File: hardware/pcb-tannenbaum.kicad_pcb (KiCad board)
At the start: 2 copper layers, 70 x 89 mm, 30 parts, among them J1 Conn_02x03_Counter_Clockwise, SW1 SW_Push, SW2 SW_Push, U1 TMP101, U2 ATtiny85V-10SU, U3 TPS27081A_ForReversePolarityP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

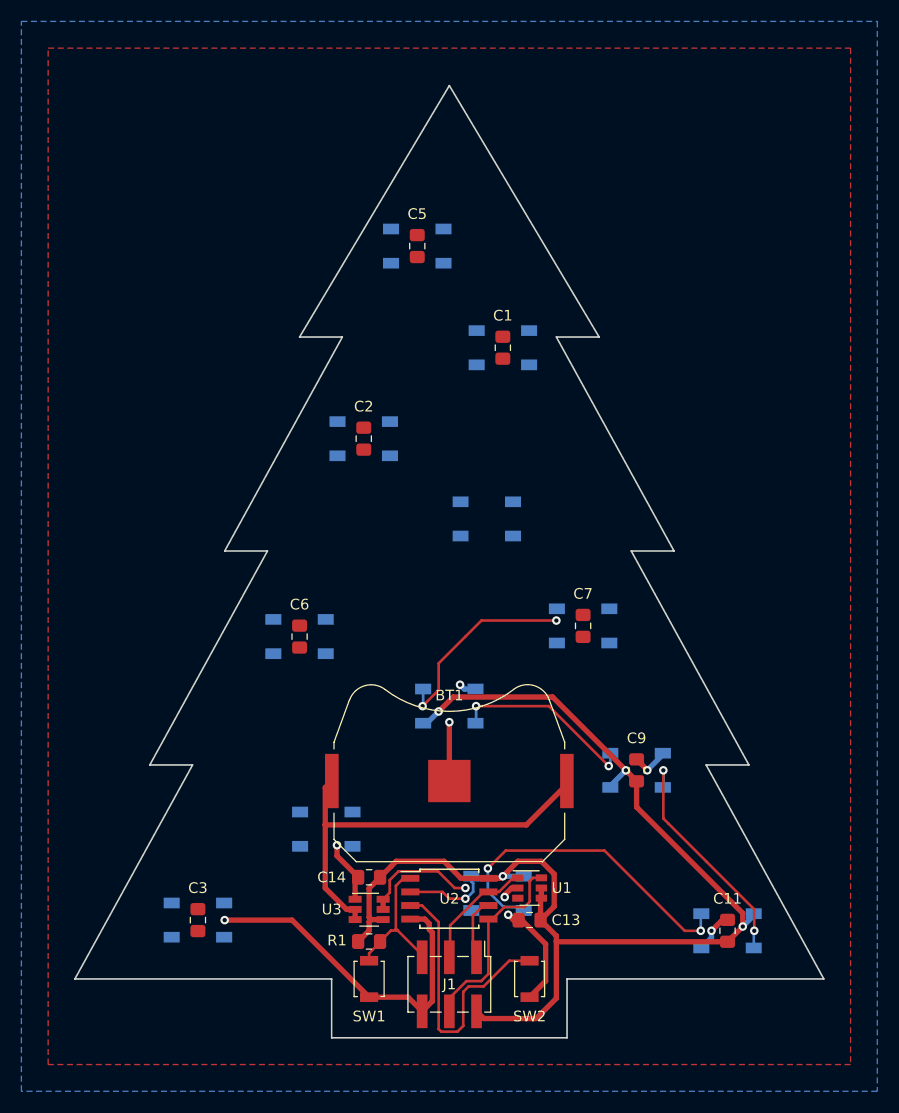
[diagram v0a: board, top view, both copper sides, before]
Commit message: Finish first iteration of PCB layout
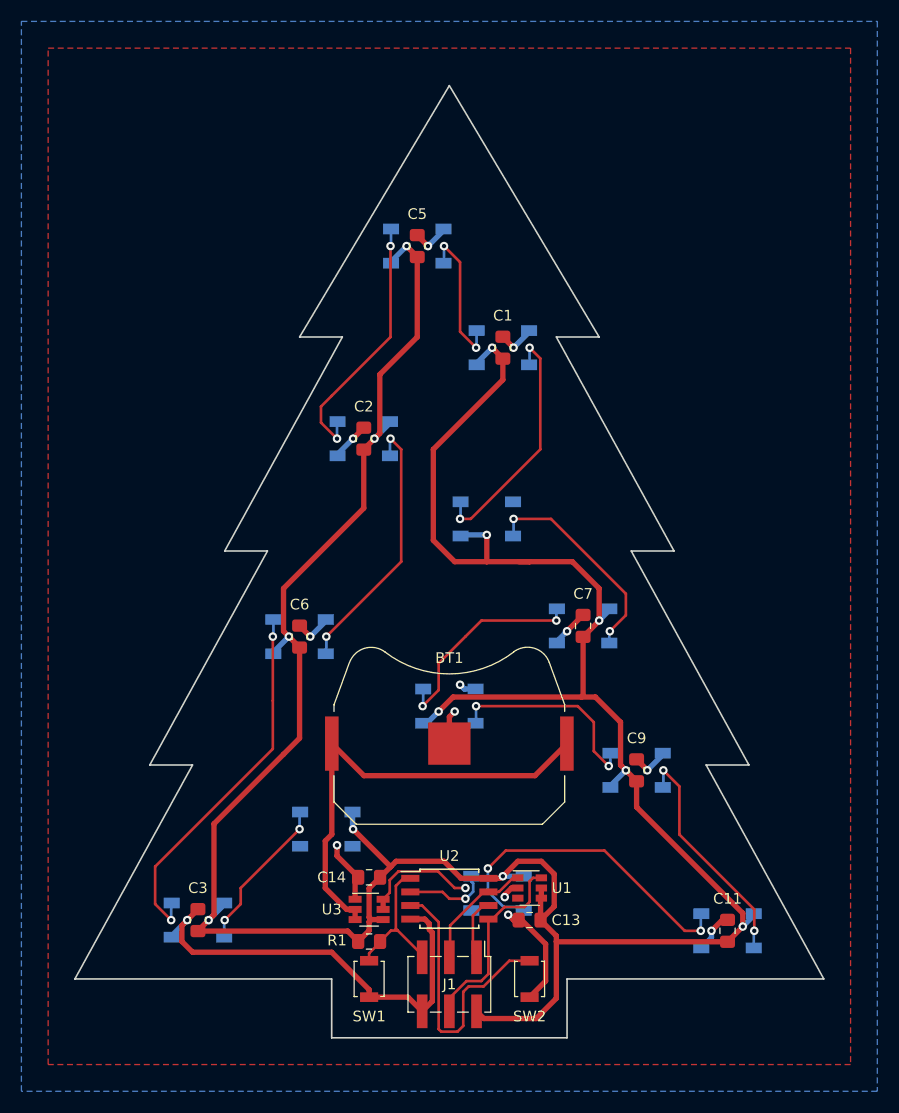
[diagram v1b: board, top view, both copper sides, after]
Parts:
- moved BT1 3.50 mm to (155.0, 107.5)
- turned D12 to 180 degrees
- turned D2 to 180 degrees
- turned D3 to 180 degrees
- turned D7 to 180 degrees
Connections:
- C2 pad 1: Net-(C2-Pad1) -> VCC
- C2 pad 2: Net-(C2-Pad2) -> GND
- C3 pad 1: Net-(C3-Pad1) -> VCC
- C3 pad 2: Net-(C3-Pad2) -> GND
- C5 pad 1: Net-(C5-Pad1) -> VCC
- C5 pad 2: Net-(C5-Pad2) -> GND
- C6 pad 1: Net-(C6-Pad1) -> VCC
- C6 pad 2: Net-(C6-Pad2) -> GND
- C7 pad 1: Net-(C7-Pad1) -> VCC
- C7 pad 2: Net-(C7-Pad2) -> GND
- D12 pad 1: Net-(D12-Pad1) -> VCC
- D12 pad 3: Net-(D12-Pad3) -> GND
- D2 pad 1: Net-(D2-Pad1) -> VCC
- D2 pad 3: Net-(D2-Pad3) -> GND
- D3 pad 1: Net-(D3-Pad1) -> VCC
- D3 pad 2: Net-(D3-Pad2) -> Net-(D12-Pad4)
- D3 pad 3: Net-(D3-Pad3) -> GND
- D4 pad 1: Net-(D4-Pad1) -> VCC
- D4 pad 2: Net-(D4-Pad2) -> Net-(D1-Pad4)
- D4 pad 3: Net-(D4-Pad3) -> GND
- D5 pad 1: Net-(D5-Pad1) -> VCC
- D5 pad 2: Net-(D5-Pad2) -> Net-(D2-Pad4)
- D5 pad 3: Net-(D5-Pad3) -> GND
- D5 pad 4: Net-(D5-Pad4) -> Net-(D1-Pad2)
- D6 pad 1: Net-(D6-Pad1) -> VCC
- D6 pad 2: Net-(D6-Pad2) -> Net-(D3-Pad4)
- D6 pad 3: Net-(D6-Pad3) -> GND
- D6 pad 4: Net-(D6-Pad4) -> Net-(D2-Pad2)
- D7 pad 1: Net-(D7-Pad1) -> VCC
- D7 pad 2: Net-(D7-Pad2) -> Net-(D4-Pad4)
- D7 pad 3: Net-(D7-Pad3) -> GND
- D8 pad 2: Net-(D8-Pad2) -> Net-(D7-Pad4)
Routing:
- net VCC: track 117.3 -> 283.5 mm, vias 4 -> 12
- net Net-(D3-Pad4): track 0.00 -> 34.9 mm, vias 0 -> 2
- net GND: track 76.3 -> 101.6 mm, vias 9 -> 14
- net Net-(D2-Pad2): track 0.00 -> 25.1 mm, vias 0 -> 2
- net Net-(D2-Pad4): track 0.00 -> 24.6 mm, vias 0 -> 2
- net Net-(D1-Pad4): track 0.00 -> 23.3 mm, vias 0 -> 2
- net Net-(D4-Pad4): track 0.00 -> 20.3 mm, vias 0 -> 2
- net Net-(D7-Pad4): track 0.00 -> 20.0 mm, vias 0 -> 2
- net Net-(D8-Pad2): track 18.9 -> 0.00 mm, vias 2 -> 0
- net Net-(D12-Pad4): track 0.00 -> 14.6 mm, vias 0 -> 2
- net Net-(D1-Pad2): track 0.00 -> 14.0 mm, vias 0 -> 2
- net Net-(BT1-Pad1): track 39.3 -> 42.8 mm
- net Net-(D8-Pad4): track 17.6 -> 19.2 mm

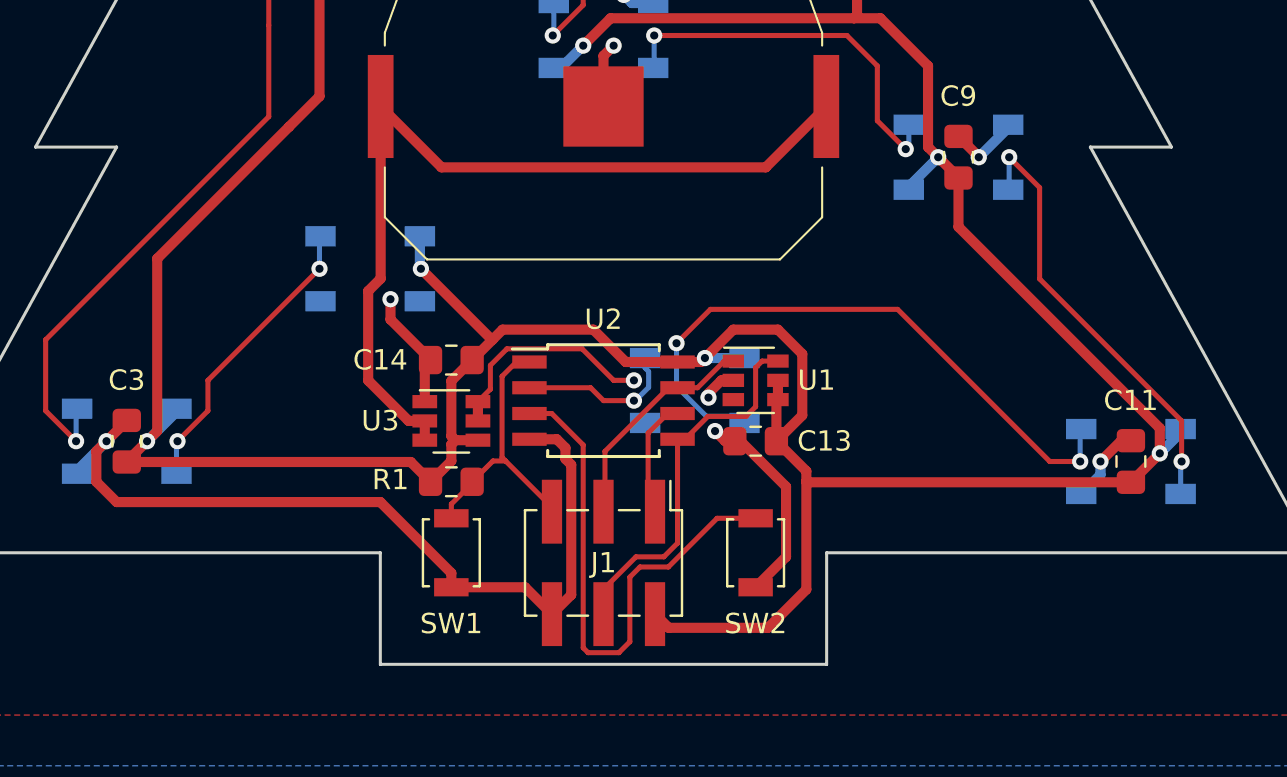
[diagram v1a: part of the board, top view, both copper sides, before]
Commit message: Switch to STM MCU
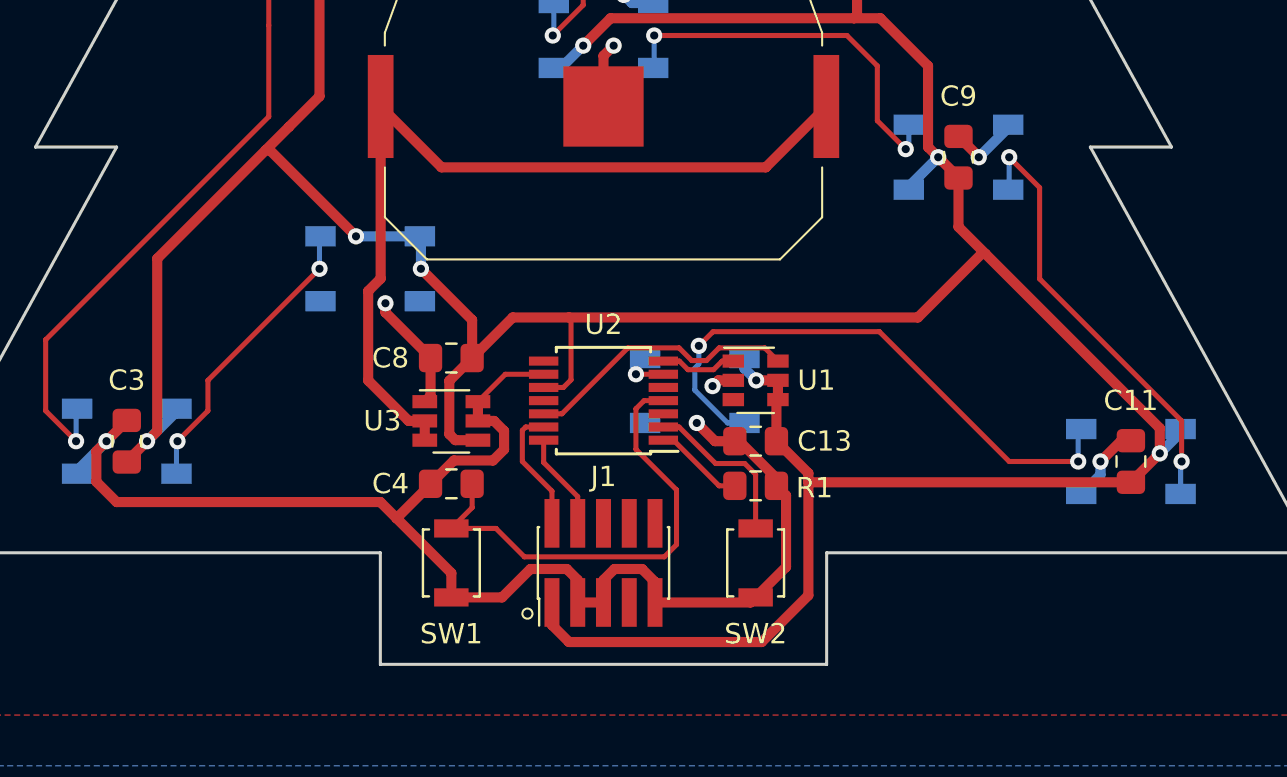
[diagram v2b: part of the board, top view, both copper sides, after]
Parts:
- removed C14: C, Capacitor_SMD:C_0805_2012Metric_Pad1.15x1.40mm_HandSolder
- added C4: C, Capacitor_SMD:C_0805_2012Metric_Pad1.15x1.40mm_HandSolder, F.Cu at (147.5, 126.1)
- added C8: C, Capacitor_SMD:C_0805_2012Metric_Pad1.15x1.40mm_HandSolder, F.Cu at (147.5, 119.9)
- J1: value Conn_02x03_Counter_Clockwise -> Conn_ARM_JTAG_SWD_10; footprint Connector_PinHeader_2.54mm:PinHeader_2x03_P2.54mm_Vertical_SMD -> Connector_PinHeader_1.27mm:PinHeader_2x05_P1.27mm_Vertical_SMD
- U2: value ATtiny85V-10SU -> STM32L011D3Px; footprint Package_SO:SOIJ-8_5.3x5.3mm_P1.27mm -> Package_SO:TSSOP-14_4.4x5mm_P0.65mm
- moved R1 15.0 mm to (162.5, 126.2)
- moved SW1 0.50 mm to (147.5, 130.0)
- moved SW2 0.50 mm to (162.5, 130.0)
- turned J1 to 90 degrees
- turned U2 to 180 degrees
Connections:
- J1 pad 1: MISO -> VCC
- J1 pad 2: VCC -> SWDIO
- J1 pad 3: SCL_SCK -> GND
- J1 pad 4: SDA_MOSI -> SWCLK
- J1 pad 5: NRST -> GND
- J1 pad 6: GND -> Net-(J1-Pad6)
- R1 pad 1: VCC -> Net-(R1-Pad1)
- R1 pad 2: NRST -> GND
- U1 pad 1: SCL_SCK -> SCL
- U1 pad 6: SDA_MOSI -> SDA
- U2 pad 1: NRST -> Net-(R1-Pad1)
- U2 pad 2: DIN -> Net-(SW2-Pad1)
- U2 pad 3: Net-(SW2-Pad1) -> Net-(U2-Pad3)
- U2 pad 4: GND -> NRST
- U2 pad 5: SDA_MOSI -> Net-(U2-Pad5)
- U2 pad 6: MISO -> DIN
- U2 pad 7: SCL_SCK -> SCL
- U2 pad 8: VCC -> Net-(U2-Pad8)
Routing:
- net SDA_MOSI: track 18.6 -> 0.00 mm
- net Net-(SW2-Pad1): track 26.5 -> 8.18 mm
- net SDA: track 0.00 -> 13.7 mm
- net SCL_SCK: track 11.2 -> 0.00 mm
- net NRST: track 13.6 -> 23.6 mm
- net VCC: track 283.5 -> 291.4 mm, vias 12 -> 13
- net GND: track 101.6 -> 108.8 mm, vias 14 -> 13
- net SWDIO: track 0.00 -> 6.31 mm
- net MISO: track 5.87 -> 0.00 mm
- net DIN: track 7.93 -> 2.34 mm
- net SWCLK: track 0.00 -> 4.80 mm
- net Net-(R1-Pad1): track 0.00 -> 4.46 mm
- net SCL: track 0.00 -> 3.90 mm
- net Net-(D10-Pad2): track 31.5 -> 28.7 mm

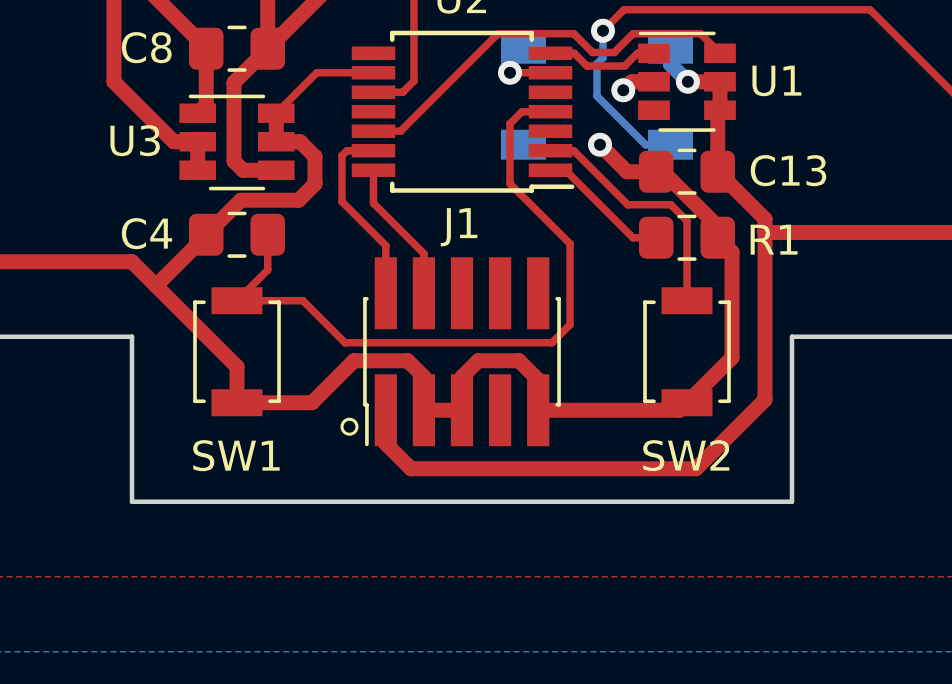
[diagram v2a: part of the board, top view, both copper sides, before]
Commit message: Add cube project, change buttons
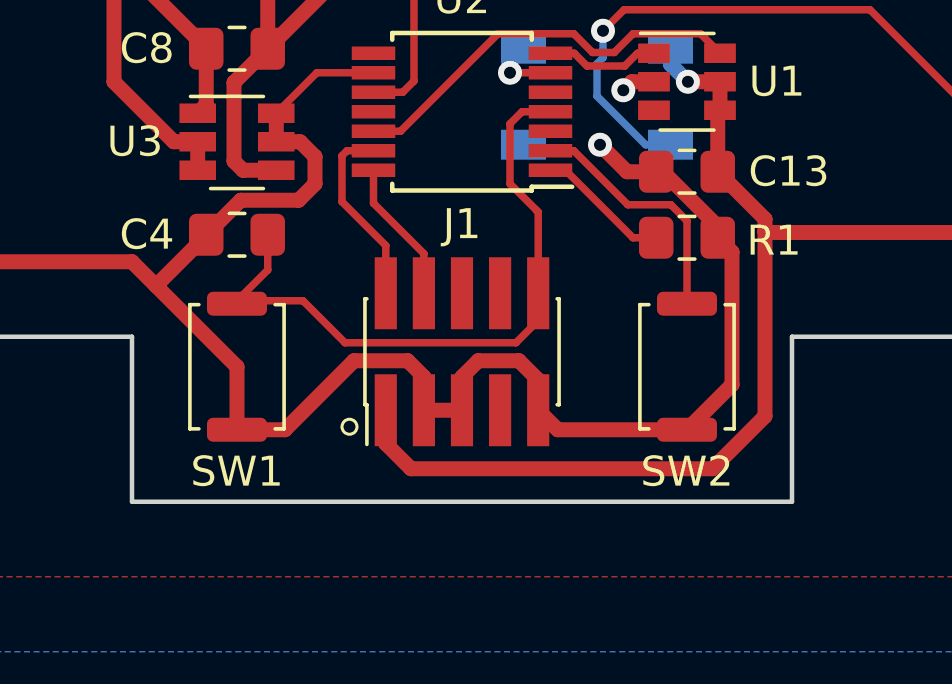
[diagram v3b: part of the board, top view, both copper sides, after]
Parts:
- SW1, SW2: footprint Button_Switch_SMD:SW_SPST_B3U-1000P -> Button_Switch_SMD:SW_Push_SPST_NO_Alps_SKRK
- moved SW1 0.50 mm to (147.5, 130.5)
- moved SW2 0.50 mm to (162.5, 130.5)
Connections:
- J1 pad 10: Net-(J1-Pad10) -> NRST
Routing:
- net GND: track 108.8 -> 111.6 mm
- net NRST: track 23.6 -> 22.0 mm
